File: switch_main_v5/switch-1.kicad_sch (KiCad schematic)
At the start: 42 parts, among them U1601 SJA1105QELY, Y1601 XRCGB25M000F3A16R0

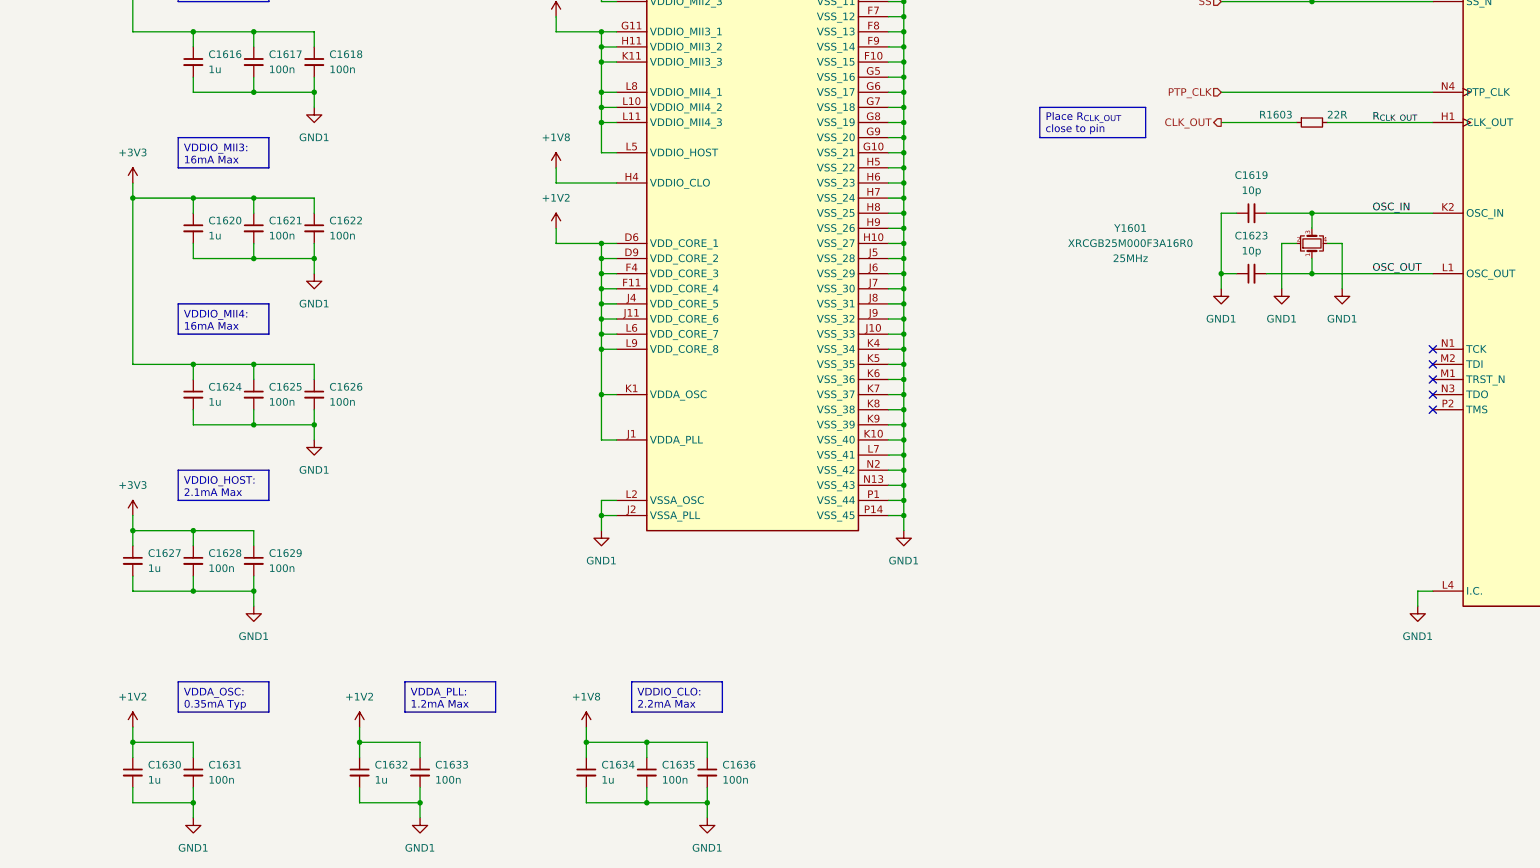
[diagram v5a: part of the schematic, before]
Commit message: Removed one switch crystal so both are now clocked from the same source and timestamps won't drift
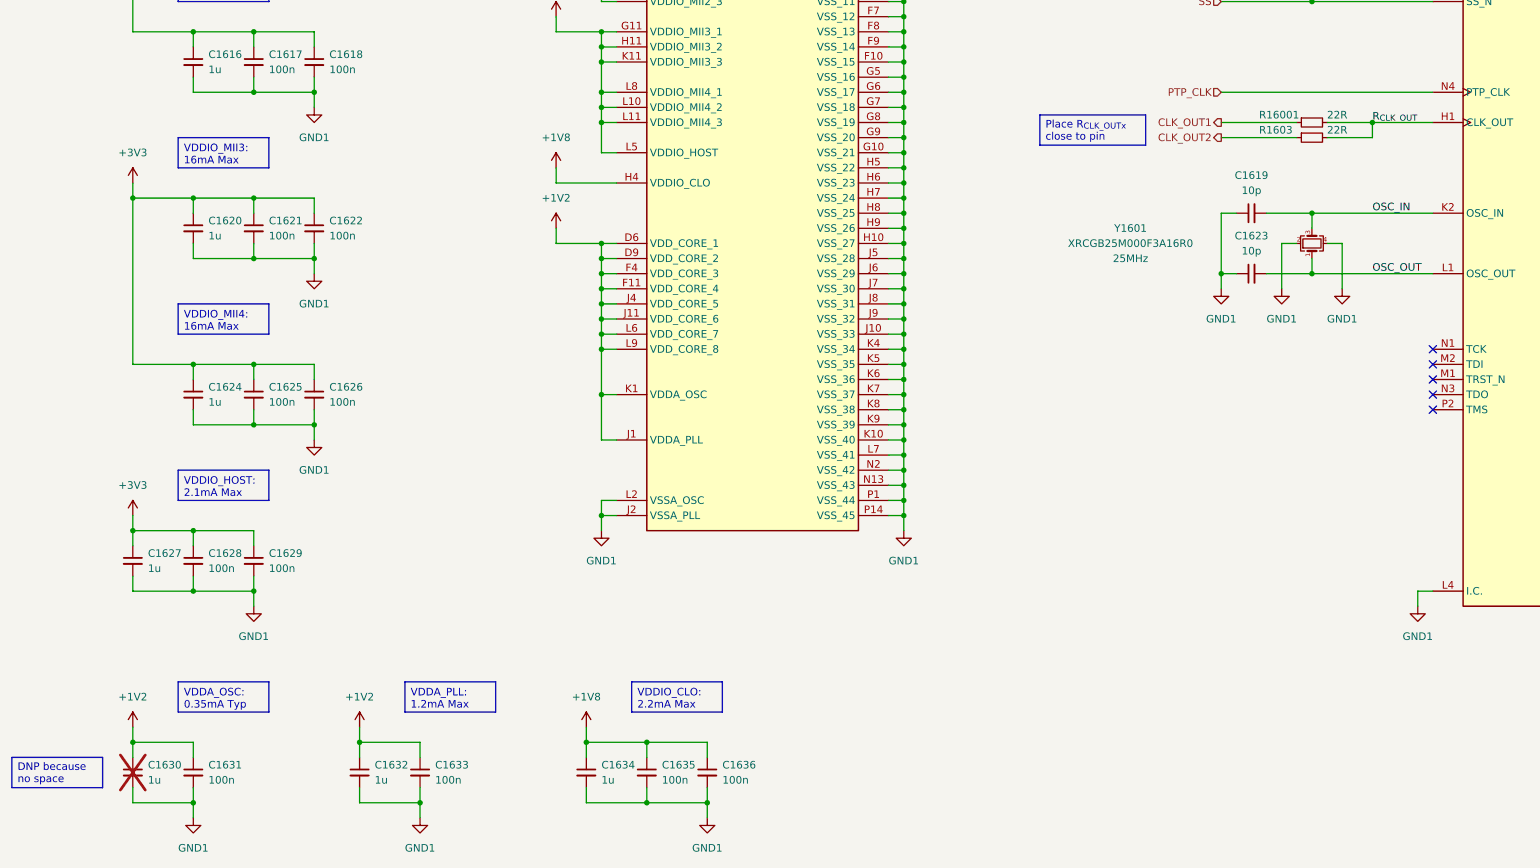
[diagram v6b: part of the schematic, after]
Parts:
- added R16001: 22R, Resistor_SMD:R_0402_1005Metric, symbol Device:R_Small
- C1630: now not fitted; now left out of the parts list
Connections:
- net R_{CLK_OUT}: now also R16001.2
- net CLK_OUT renamed CLK_OUT2
- new net CLK_OUT1: R16001.1
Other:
- moved on the sheet: R1603
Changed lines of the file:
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@@
 		)
 	)
+	(text_box "DNP because no space"
+		(exclude_from_sim no)
+		(at 17.78 248.92 0)
+		(size 15.24 5.08)
+		(margins 0.9525 0.9525 0.9525 0.9525)
+		(stroke
+			(width 0)
+			(type solid)
+		)
+		(fill
+			(type none)
+		)
+		(effects
+			(font
+				(size 1.27 1.27)
+			)
+			(justify left)
+		)
+	)
 	(text_box "VDDIO_MII0:\n46mA Max"
 		(exclude_from_sim no)
@@
 		)
 	)
-	(text_box "Place R_{CLK_OUT} close to pin"
+	(text_box "Place R_{CLK_OUTx} close to pin"
 		(exclude_from_sim no)
-		(at 190.5 139.7 0)
+		(at 190.5 140.97 0)
 		(size 17.78 5.08)
 		(margins 0.9525 0.9525 0.9525 0.9525)
@@
 	)
 	(junction
+		(at 246.38 142.24)
+		(diameter 0)
+		(color 0 0 0 0)
+	)
+	(junction
 		(at 167.64 187.96)
 		(diameter 0)
@@
 		)
 	)
+	(wire
+		(pts
+			(xy 238.76 144.78) (xy 246.38 144.78)
+		)
+		(stroke
+			(width 0)
+			(type default)
+		)
+	)
 	(bus
 		(pts
@@
 	(wire
 		(pts
+			(xy 220.98 144.78) (xy 233.68 144.78)
+		)
+		(stroke
+			(width 0)
+			(type default)
+		)
+	)
+	(wire
+		(pts
 			(xy 109.22 127) (xy 116.84 127)
 		)
@@
 	(wire
 		(pts
-			(xy 238.76 142.24) (xy 256.54 142.24)
+			(xy 238.76 142.24) (xy 246.38 142.24)
 		)
 		(stroke
@@
 	(wire
 		(pts
+			(xy 246.38 144.78) (xy 246.38 142.24)
+		)
+		(stroke
+			(width 0)
+			(type default)
+		)
+	)
+	(wire
+		(pts
 			(xy 167.64 172.72) (xy 165.1 172.72)
 		)
@@
 	(wire
 		(pts
+			(xy 246.38 142.24) (xy 256.54 142.24)
+		)
+		(stroke
+			(width 0)
+			(type default)
+		)
+	)
+	(wire
+		(pts
 			(xy 116.84 187.96) (xy 116.84 195.58)
 		)
@@
 		)
 	)
-	(hierarchical_label "CLK_OUT"
+	(hierarchical_label "CLK_OUT1"
 		(shape output)
 		(at 220.98 142.24 180)
@@
 		)
 	)
+	(hierarchical_label "CLK_OUT2"
+		(shape output)
+		(at 220.98 144.78 180)
+		(effects
+			(font
+				(size 1.27 1.27)
+			)
+			(justify right)
+		)
+	)
 	(hierarchical_label "xMII2{RGMII}"
 		(shape bidirectional)
@@
 		(polyline
 			(pts
-				(xy 226.06 134.62) (xy 243.84 134.62) (xy 243.84 144.78) (xy 226.06 144.78)
+				(xy 226.06 134.62) (xy 243.84 134.62) (xy 243.84 147.32) (xy 226.06 147.32)
 			)
 			(stroke
@@
 	(symbol
 		(lib_id "Device:R_Small")
-		(at 236.22 142.24 90)
+		(at 236.22 144.78 90)
 		(mirror x)
 		(unit 1)
@@
 		(dnp no)
 		(property "Reference" "R1603"
-			(at 227.33 140.97 90)
+			(at 227.33 143.51 90)
 			(effects
 				(font
@@
 		)
 		(property "Value" "22R"
-			(at 238.76 140.97 90)
+			(at 238.76 143.51 90)
 			(effects
 				(font
@@
 		)
 		(property "Footprint" "Resistor_SMD:R_0402_1005Metric"
-			(at 236.22 142.24 0)
+			(at 236.22 144.78 0)
 			(effects
 				(font
@@
 		)
 		(property "Datasheet" "~"
-			(at 236.22 142.24 0)
+			(at 236.22 144.78 0)
 			(effects
 				(font
@@
 		)
 		(property "Description" "Resistor, small symbol"
-			(at 236.22 142.24 0)
+			(at 236.22 144.78 0)
 			(effects
 				(font
@@
 		(unit 1)
 		(exclude_from_sim no)
-		(in_bom yes)
-		(on_board yes)
-		(dnp no)
+		(in_bom no)
+		(on_board no)
+		(dnp yes)
 		(property "Reference" "C1630"
 			(at 40.64 250.1962 0)
@@
 					(unit 1)
 				)
+			)
+		)
+	)
+	(symbol
+		(lib_id "Device:R_Small")
+		(at 236.22 142.24 90)
+		(mirror x)
+		(unit 1)
+		(exclude_from_sim no)
+		(in_bom yes)
+		(on_board yes)
+		(dnp no)
+		(property "Reference" "R16001"
+			(at 227.33 140.97 90)
+			(effects
+				(font
+					(size 1.27 1.27)
+				)
+				(justify right)
+			)
+		)
+		(property "Value" "22R"
+			(at 238.76 140.97 90)
+			(effects
+				(font
+					(size 1.27 1.27)
+				)
+				(justify right)
+			)
+		)
+		(property "Footprint" "Resistor_SMD:R_0402_1005Metric"
+			(at 236.22 142.24 0)
+			(effects
+				(font
+					(size 1.27 1.27)
+				)
+				(hide yes)
+			)
+		)
+		(property "Datasheet" "~"
+			(at 236.22 142.24 0)
+			(effects
+				(font
+					(size 1.27 1.27)
+				)
+				(hide yes)
+			)
+		)
+		(property "Description" "Resistor, small symbol"
+			(at 236.22 142.24 0)
+			(effects
+				(font
+					(size 1.27 1.27)
+				)
+				(hide yes)
+			)
+		)
+		(pin "2"
+		)
+		(pin "1"
+		)
+		(instances
+			(project "switch_main_v5"
+				(path "/a5e57332-4284-4d3c-ab3c-13bc0ddb29b6/31c4512b-1e39-4437-8559-238fb7009a56"
+					(reference "R16001")
+					(unit 1)
+				)
